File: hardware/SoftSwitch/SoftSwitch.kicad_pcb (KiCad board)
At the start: 2 copper layers, 41.9 x 52.1 mm, 17 parts, among them J1 80-COLUMN IN, J2 APPLE VIDEO, J3 5-PRONG OUTPUT, J4 4-PRONG OUTPUT, Q1 3904, Q2 3906, U1 74LS259, U2 74LS259 (passthrough header)

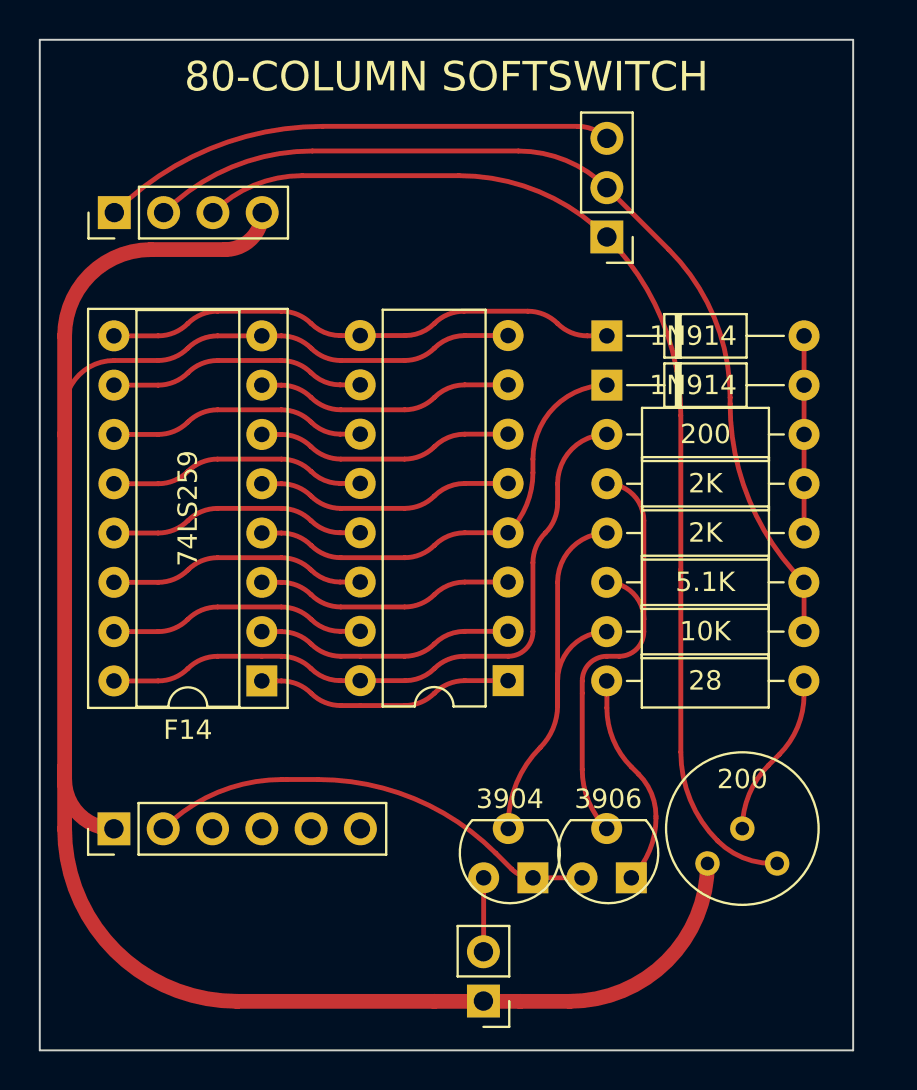
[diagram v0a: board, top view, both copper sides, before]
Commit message: make softswitch narrower, general improvements
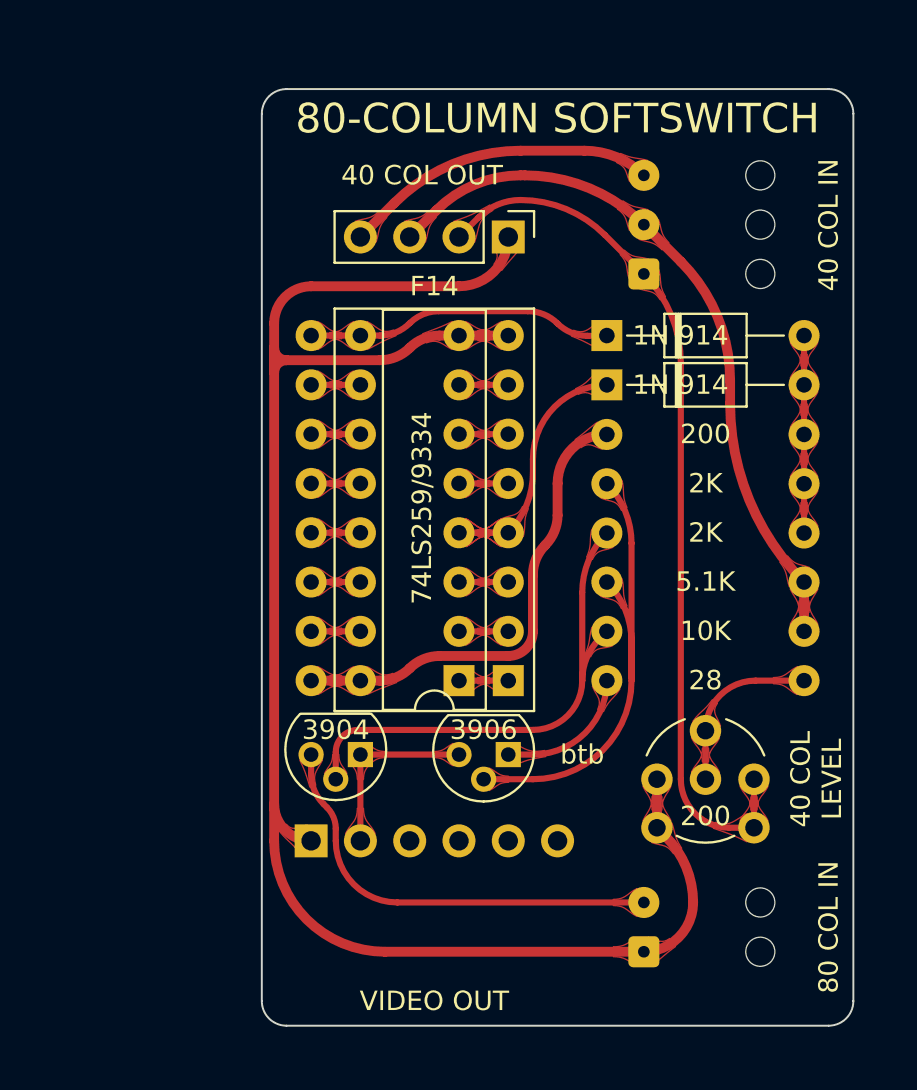
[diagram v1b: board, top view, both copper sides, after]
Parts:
- D1, D2: value 1N914 -> 1N 914
- F14: renamed from U1; value 74LS259 -> 74LS259/9334
- FP14: renamed from U2; value 74LS259 (passthrough header) -> F14 passthrough; footprint Package_DIP:DIP-16_W7.62mm -> Package_DIP:DIP-16_W7.62mm_Socket
- J1: value 80-COLUMN IN -> 80 COL IN; footprint Connector_PinHeader_2.54mm:PinHeader_1x02_P2.54mm_Vertical -> Connector_Wire:SolderWire-0.1sqmm_1x02_P3.6mm_D0.4mm_OD1mm_Relief
- J2: value APPLE VIDEO -> 40 COL IN; footprint Connector_PinHeader_2.54mm:PinHeader_1x03_P2.54mm_Vertical -> Connector_Wire:SolderWire-0.1sqmm_1x03_P3.6mm_D0.4mm_OD1mm_Relief
- J3: value 5-PRONG OUTPUT -> VIDEO OUT; footprint Connector_PinHeader_2.54mm:PinHeader_1x06_P2.54mm_Vertical -> Connector_PinHeader_2.54mm:PinHeader_1x06_P2.54mm_Horizontal
- J4: value 4-PRONG OUTPUT -> 40 COL OUT
- Q1, Q2: footprint MyTransistor:TO-92_oldstyle -> Package_TO_SOT_THT:TO-92
- RV1: footprint Potentiometer_THT:Potentiometer_Bourns_3339H_Vertical -> MyPotentiometer:Multi_Potentiometer_6mm_Vertical
- moved J3 22.9 mm to (77.5, 99.7), turned to -90 degrees
- moved J4 20.3 mm to (74.9, 68.6), turned to -90 degrees
- moved F14 12.7 mm to (74.9, 91.4)
- moved Q1 10.2 mm to (67.3, 95.2)
- moved J1 8.65 mm to (81.9, 105.4), turned to 90 degrees
- moved Q2 8.12 mm to (74.9, 95.2)
- moved J2 2.69 mm to (81.9, 70.5), turned to 90 degrees
- moved FP14 2.53 mm to (72.4, 91.4)
- moved RV1 2.19 mm to (87.6, 99.0)
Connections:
- J4 pad 1: /+12V -> GND
- J4 pad 2: /-5V -> Net-(J2-Pad1)
- J4 pad 3: Net-(J2-Pad1) -> /-5V
- J4 pad 4: GND -> /+12V
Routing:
- net GND: track 111.5 -> 91.8 mm
- net Net-(J1-Pad2): track 3.82 -> 22.4 mm
- net /SWITCHED VIDEO OUT: track 23.6 -> 9.52 mm
- net /-5V: track 50.0 -> 37.1 mm
- net Net-(J2-Pad1): track 57.5 -> 45.6 mm
- net +5V: track 35.0 -> 24.2 mm
- net Net-(D2-Pad1): track 26.7 -> 15.9 mm
- net Net-(F14-Pad1): track 13.3 -> 2.54 mm
- net Net-(F14-Pad6): track 13.3 -> 2.54 mm
- net Net-(F14-Pad2): track 13.3 -> 2.54 mm
- net Net-(F14-Pad5): track 13.3 -> 2.54 mm
- net Net-(F14-Pad3): track 13.3 -> 2.54 mm
- net Net-(F14-Pad7): track 13.3 -> 2.54 mm
- net Net-(F14-Pad15): track 13.3 -> 2.54 mm
- net Net-(F14-Pad13): track 13.3 -> 2.54 mm
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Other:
- board size 41.9 x 52.1 mm -> 30.5 x 48.3 mm
- board text added: "40 COL LEVEL"
- board text added: "btb"
